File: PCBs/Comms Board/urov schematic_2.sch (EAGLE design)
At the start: 18 parts

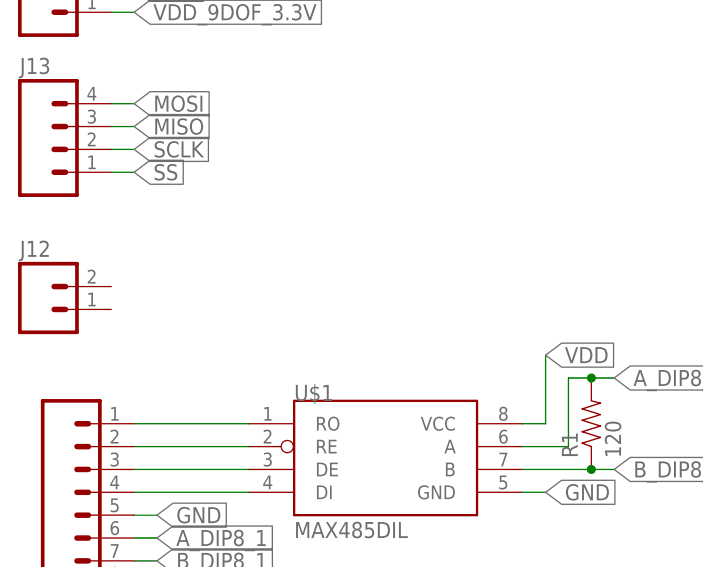
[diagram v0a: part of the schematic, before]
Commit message: Adding jumpers to select I2C or SPI
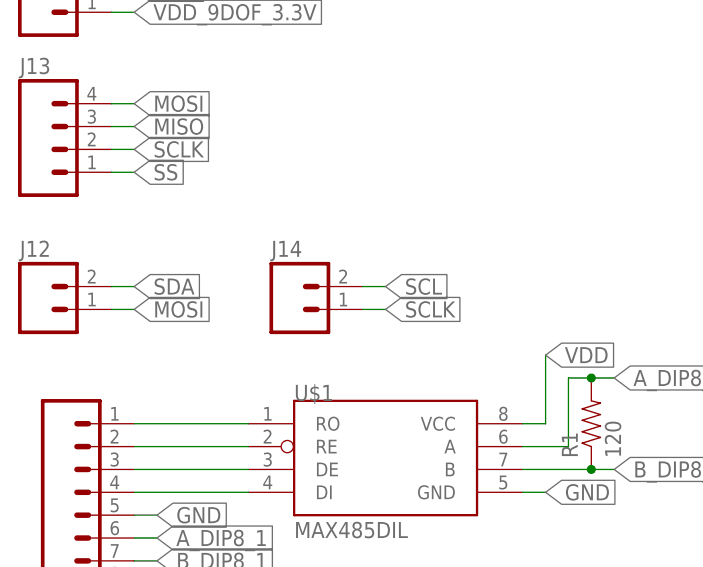
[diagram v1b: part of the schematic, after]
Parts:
- added J14: (no value), SparkFun-Connectors:M02PTH
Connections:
- net MOSI: now also J12.1
- net SCL: now also J14.2
- net SCLK: now also J14.1
- net SDA: now also J12.2
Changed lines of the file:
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@@
 <part name="PRESSURE_INTERNAL" library="SparkFun-Sensors" deviceset="MS5803-14BA" device=""/>
 <part name="J13" library="SparkFun-Connectors" deviceset="M04" device="PTH"/>
+<part name="J14" library="SparkFun-Connectors" deviceset="M02" device="PTH"/>
 </parts>
 <sheets>
@@
 <instance part="PRESSURE_INTERNAL" gate="G$1" x="-86.36" y="55.88"/>
 <instance part="J13" gate="G$1" x="-182.88" y="50.8"/>
+<instance part="J14" gate="G$1" x="-157.48" y="33.02"/>
 </instances>
 <busses>
@@
 <label x="-93.98" y="63.5" size="1.778" layer="95" rot="R180" xref="yes"/>
 </segment>
+<segment>
+<pinref part="J14" gate="G$1" pin="2"/>
+<wire x1="-149.86" y1="35.56" x2="-147.32" y2="35.56" width="0.1524" layer="91"/>
+<label x="-147.32" y="35.56" size="1.778" layer="95" xref="yes"/>
+</segment>
 </net>
 <net name="SDA" class="0">
@@
 <label x="-175.26" y="71.12" size="1.778" layer="95" xref="yes"/>
 </segment>
+<segment>
+<pinref part="J12" gate="G$1" pin="2"/>
+<wire x1="-177.8" y1="35.56" x2="-175.26" y2="35.56" width="0.1524" layer="91"/>
+<label x="-175.26" y="35.56" size="1.778" layer="95" xref="yes"/>
+</segment>
 </net>
 <net name="VDD_9DOF_3.3V" class="0">
@@
 <label x="-175.26" y="55.88" size="1.778" layer="95" xref="yes"/>
 </segment>
+<segment>
+<pinref part="J12" gate="G$1" pin="1"/>
+<wire x1="-175.26" y1="33.02" x2="-177.8" y2="33.02" width="0.1524" layer="91"/>
+<label x="-175.26" y="33.02" size="1.778" layer="95" xref="yes"/>
+</segment>
 </net>
 <net name="SCLK" class="0">
@@
 <label x="-175.26" y="50.8" size="1.778" layer="95" xref="yes"/>
 </segment>
-</net>
+<segment>
+<pinref part="J14" gate="G$1" pin="1"/>
+<wire x1="-147.32" y1="33.02" x2="-149.86" y2="33.02" width="0.1524" layer="91"/>
+<label x="-147.32" y="33.02" size="1.778" layer="95" xref="yes"/>
+</segment>
+</net>
